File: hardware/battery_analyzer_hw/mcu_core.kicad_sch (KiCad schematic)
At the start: 10 parts, among them SW1 SW_Push, SW2 SW_Push, U3 ESP32-S3-WROOM-1

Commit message: feat(hw): add RJ45 slave ports, isolated 1-Wire and PWM routing fix(hw): split I2C into UI and PWR buses to prevent PID blocking
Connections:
- net 1W_CH0: now reaches U3.12 (IO8)
- net 1W_CH1: now reaches U3.17 (IO9)
- net 1W_CH2: now reaches U3.18 (IO10)
- net 1W_CH3: now reaches U3.19 (IO11)
- net ADC_ALERT: now reaches U3.24 (IO47)
- net PWM_CH0: now reaches U3.31 (IO38)
- net PWM_CH1: now reaches U3.32 (IO39)
- net PWM_CH2: now reaches U3.33 (IO40)
- net PWM_CH3: now reaches U3.34 (IO41)
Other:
- moved on the sheet: R5, R6
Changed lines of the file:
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@@
+	(wire
+		(pts
+			(xy 143.51 110.49) (xy 151.13 110.49)
+		)
+		(stroke
+			(width 0)
+			(type default)
+		)
+	)
+	(wire
+		(pts
+			(xy 143.51 105.41) (xy 151.13 105.41)
+		)
+		(stroke
+			(width 0)
+			(type default)
+		)
+	)
 	(wire
 		(pts
@@
 	(wire
 		(pts
-			(xy 196.85 133.35) (xy 196.85 118.11)
-		)
-		(stroke
-			(width 0)
-			(type default)
-		)
-	)
-	(wire
-		(pts
-			(xy 191.77 133.35) (xy 191.77 120.65)
+			(xy 222.25 134.62) (xy 222.25 118.11)
+		)
+		(stroke
+			(width 0)
+			(type default)
+		)
+	)
+	(wire
+		(pts
+			(xy 217.17 134.62) (xy 217.17 120.65)
 		)
 		(stroke
@@
 	(wire
 		(pts
+			(xy 181.61 110.49) (xy 190.5 110.49)
+		)
+		(stroke
+			(width 0)
+			(type default)
+		)
+	)
+	(wire
+		(pts
 			(xy 115.57 74.93) (xy 115.57 82.55)
 		)
@@
 	(wire
 		(pts
-			(xy 191.77 140.97) (xy 191.77 153.67)
+			(xy 217.17 142.24) (xy 217.17 154.94)
 		)
 		(stroke
@@
 	(wire
 		(pts
+			(xy 181.61 105.41) (xy 190.5 105.41)
+		)
+		(stroke
+			(width 0)
+			(type default)
+		)
+	)
+	(wire
+		(pts
 			(xy 115.57 45.72) (xy 115.57 46.99)
 		)
@@
 	(wire
 		(pts
+			(xy 181.61 113.03) (xy 190.5 113.03)
+		)
+		(stroke
+			(width 0)
+			(type default)
+		)
+	)
+	(wire
+		(pts
 			(xy 143.51 123.19) (xy 151.13 123.19)
 		)
@@
 	(wire
 		(pts
-			(xy 196.85 118.11) (xy 181.61 118.11)
+			(xy 143.51 107.95) (xy 151.13 107.95)
+		)
+		(stroke
+			(width 0)
+			(type default)
+		)
+	)
+	(wire
+		(pts
+			(xy 222.25 118.11) (xy 181.61 118.11)
 		)
 		(stroke
@@
 	(wire
 		(pts
-			(xy 191.77 120.65) (xy 181.61 120.65)
+			(xy 217.17 120.65) (xy 181.61 120.65)
 		)
 		(stroke
@@
 	(wire
 		(pts
-			(xy 196.85 140.97) (xy 196.85 153.67)
+			(xy 181.61 107.95) (xy 190.5 107.95)
+		)
+		(stroke
+			(width 0)
+			(type default)
+		)
+	)
+	(wire
+		(pts
+			(xy 143.51 113.03) (xy 151.13 113.03)
+		)
+		(stroke
+			(width 0)
+			(type default)
+		)
+	)
+	(wire
+		(pts
+			(xy 222.25 142.24) (xy 222.25 154.94)
 		)
 		(stroke
@@
 		(pts
 			(xy 109.22 57.15) (xy 102.87 57.15)
+		)
+		(stroke
+			(width 0)
+			(type default)
+		)
+	)
+	(wire
+		(pts
+			(xy 181.61 123.19) (xy 189.23 123.19)
 		)
 		(stroke
@@
 		)
 	)
+	(hierarchical_label "PWM_CH0"
+		(shape bidirectional)
+		(at 190.5 105.41 0)
+		(effects
+			(font
+				(size 1.27 1.27)
+			)
+			(justify left)
+		)
+	)
 	(hierarchical_label "ENC_B"
 		(shape bidirectional)
@@
 		)
 	)
+	(hierarchical_label "PWM_CH1"
+		(shape bidirectional)
+		(at 190.5 107.95 0)
+		(effects
+			(font
+				(size 1.27 1.27)
+			)
+			(justify left)
+		)
+	)
+	(hierarchical_label "1W_CH0"
+		(shape bidirectional)
+		(at 143.51 105.41 180)
+		(effects
+			(font
+				(size 1.27 1.27)
+			)
+			(justify right)
+		)
+	)
 	(hierarchical_label "BTN_TARE"
 		(shape bidirectional)
@@
 		)
 	)
+	(hierarchical_label "1W_CH3"
+		(shape bidirectional)
+		(at 143.51 113.03 180)
+		(effects
+			(font
+				(size 1.27 1.27)
+			)
+			(justify right)
+		)
+	)
 	(hierarchical_label "USB_D-"
 		(shape bidirectional)
@@
 			)
 			(justify right)
+		)
+	)
+	(hierarchical_label "PWM_CH2"
+		(shape bidirectional)
+		(at 190.5 110.49 0)
+		(effects
+			(font
+				(size 1.27 1.27)
+			)
+			(justify left)
+		)
+	)
+	(hierarchical_label "1W_CH1"
+		(shape bidirectional)
+		(at 143.51 107.95 180)
+		(effects
+			(font
+				(size 1.27 1.27)
+			)
+			(justify right)
+		)
+	)
+	(hierarchical_label "ADC_ALERT"
+		(shape bidirectional)
+		(at 189.23 123.19 0)
+		(effects
+			(font
+				(size 1.27 1.27)
+			)
+			(justify left)
+		)
+	)
+	(hierarchical_label "1W_CH2"
+		(shape bidirectional)
+		(at 143.51 110.49 180)
+		(effects
+			(font
+				(size 1.27 1.27)
+			)
+			(justify right)
+		)
+	)
+	(hierarchical_label "PWM_CH3"
+		(shape bidirectional)
+		(at 190.5 113.03 0)
+		(effects
+			(font
+				(size 1.27 1.27)
+			)
+			(justify left)
 		)
 	)
@@
 	(symbol
 		(lib_id "Device:R")
-		(at 196.85 137.16 0)
+		(at 222.25 138.43 0)
 		(unit 1)
 		(body_style 1)
@@
 		(fields_autoplaced yes)
 		(property "Reference" "R5"
-			(at 199.39 135.8899 0)
+			(at 224.79 137.1599 0)
 			(show_name no)
 			(do_not_autoplace no)
@@
 		)
 		(property "Value" "10k"
-			(at 199.39 138.4299 0)
+			(at 224.79 139.6999 0)
 			(show_name no)
 			(do_not_autoplace no)
@@
 		)
 		(property "Footprint" ""
-			(at 195.072 137.16 90)
+			(at 220.472 138.43 90)
 			(hide yes)
 			(show_name no)
@@
 		)
 		(property "Datasheet" ""
-			(at 196.85 137.16 0)
+			(at 222.25 138.43 0)
 			(hide yes)
 			(show_name no)
@@
 		)
 		(property "Description" "Resistor"
-			(at 196.85 137.16 0)
+			(at 222.25 138.43 0)
 			(hide yes)
 			(show_name no)
@@
 	(symbol
 		(lib_id "power:GND")
-		(at 196.85 153.67 0)
+		(at 222.25 154.94 0)
 		(unit 1)
 		(body_style 1)
@@
 		(fields_autoplaced yes)
 		(property "Reference" "#PWR022"
-			(at 196.85 160.02 0)
+			(at 222.25 161.29 0)
 			(hide yes)
 			(show_name no)
@@
 		)
 		(property "Value" "GND"
-			(at 196.85 158.75 0)
+			(at 222.25 160.02 0)
 			(show_name no)
 			(do_not_autoplace no)
@@
 		)
 		(property "Footprint" ""
-			(at 196.85 153.67 0)
+			(at 222.25 154.94 0)
 			(hide yes)
 			(show_name no)
@@
 		)
 		(property "Datasheet" ""
-			(at 196.85 153.67 0)
+			(at 222.25 154.94 0)
 			(hide yes)
 			(show_name no)
@@
 		)
 		(property "Description" "Power symbol creates a global label with name \"GND\" , ground"
-			(at 196.85 153.67 0)
+			(at 222.25 154.94 0)
 			(hide yes)
 			(show_name no)
@@
 	(symbol
 		(lib_id "Device:R")
-		(at 191.77 137.16 0)
+		(at 217.17 138.43 0)
 		(mirror y)
 		(unit 1)
@@
 		(fields_autoplaced yes)
 		(property "Reference" "R6"
-			(at 189.23 135.8899 0)
+			(at 214.63 137.1599 0)
 			(show_name no)
 			(do_not_autoplace no)
@@
 		)
 		(property "Value" "10k"
-			(at 189.23 138.4299 0)
+			(at 214.63 139.6999 0)
 			(show_name no)
 			(do_not_autoplace no)
@@
 		)
 		(property "Footprint" ""
-			(at 193.548 137.16 90)
+			(at 218.948 138.43 90)
 			(hide yes)
 			(show_name no)
@@
 		)
 		(property "Datasheet" ""
-			(at 191.77 137.16 0)
+			(at 217.17 138.43 0)
 			(hide yes)
 			(show_name no)
@@
 		)
 		(property "Description" "Resistor"
-			(at 191.77 137.16 0)
+			(at 217.17 138.43 0)
 			(hide yes)
 			(show_name no)
@@
 	(symbol
 		(lib_id "power:GND")
-		(at 191.77 153.67 0)
+		(at 217.17 154.94 0)
 		(unit 1)
 		(body_style 1)
@@
 		(fields_autoplaced yes)
 		(property "Reference" "#PWR021"
-			(at 191.77 160.02 0)
+			(at 217.17 161.29 0)
 			(hide yes)
 			(show_name no)
@@
 		)
 		(property "Value" "GND"
-			(at 191.77 158.75 0)
+			(at 217.17 160.02 0)
 			(show_name no)
 			(do_not_autoplace no)
@@
 		)
 		(property "Footprint" ""
-			(at 191.77 153.67 0)
+			(at 217.17 154.94 0)
 			(hide yes)
 			(show_name no)
@@
 		)
 		(property "Datasheet" ""
-			(at 191.77 153.67 0)
+			(at 217.17 154.94 0)
 			(hide yes)
 			(show_name no)
@@
 		)
 		(property "Description" "Power symbol creates a global label with name \"GND\" , ground"
-			(at 191.77 153.67 0)
-			(hide yes)
-			(show_name no)
+			(at 217.17 154.94 0)
+			(hide yes)
+			(show_name no)

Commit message: refactor(hw): upgrade RJ45 to shielded, repurpose pin 1 for fan PWM fix(hw): optimize RJ45 pinout for T568B twisted pairs
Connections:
- net FAN_CH0: now reaches U3.20 (IO12)
- net FAN_CH1: now reaches U3.21 (IO13)
- net FAN_CH2: now reaches U3.22 (IO14)
- net FAN_CH3: now reaches U3.23 (IO21)
- net I2C_PWR_SDA: now reaches U3.6 (IO6)
- net I2C_PWR_SCL: now reaches U3.7 (IO7)
- net I2C_SCL renamed I2C_UI_SCL
- net I2C_SDA renamed I2C_UI_SDA
- no-connect marks 0 -> 10
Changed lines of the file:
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@@
 		(color 0 0 0 0)
 	)
+	(no_connect
+		(at 181.61 100.33)
+	)
+	(no_connect
+		(at 181.61 102.87)
+	)
+	(no_connect
+		(at 181.61 115.57)
+	)
+	(no_connect
+		(at 151.13 90.17)
+	)
+	(no_connect
+		(at 181.61 82.55)
+	)
+	(no_connect
+		(at 181.61 97.79)
+	)
+	(no_connect
+		(at 151.13 92.71)
+	)
+	(no_connect
+		(at 181.61 80.01)
+	)
+	(no_connect
+		(at 151.13 87.63)
+	)
+	(no_connect
+		(at 181.61 125.73)
+	)
 	(wire
 		(pts
@@
 	(wire
 		(pts
+			(xy 143.51 118.11) (xy 151.13 118.11)
+		)
+		(stroke
+			(width 0)
+			(type default)
+		)
+	)
+	(wire
+		(pts
 			(xy 102.87 45.72) (xy 104.14 45.72)
 		)
@@
 	(wire
 		(pts
+			(xy 143.51 120.65) (xy 151.13 120.65)
+		)
+		(stroke
+			(width 0)
+			(type default)
+		)
+	)
+	(wire
+		(pts
 			(xy 115.57 74.93) (xy 115.57 82.55)
 		)
@@
 	(wire
 		(pts
+			(xy 143.51 100.33) (xy 151.13 100.33)
+		)
+		(stroke
+			(width 0)
+			(type default)
+		)
+	)
+	(wire
+		(pts
+			(xy 143.51 102.87) (xy 151.13 102.87)
+		)
+		(stroke
+			(width 0)
+			(type default)
+		)
+	)
+	(wire
+		(pts
 			(xy 146.05 59.69) (xy 146.05 64.77)
 		)
@@
 	(wire
 		(pts
+			(xy 143.51 115.57) (xy 151.13 115.57)
+		)
+		(stroke
+			(width 0)
+			(type default)
+		)
+	)
+	(wire
+		(pts
 			(xy 105.41 97.79) (xy 105.41 107.95)
 		)
@@
 	(wire
 		(pts
+			(xy 181.61 95.25) (xy 189.23 95.25)
+		)
+		(stroke
+			(width 0)
+			(type default)
+		)
+	)
+	(wire
+		(pts
 			(xy 181.61 123.19) (xy 189.23 123.19)
 		)
@@
 		)
 	)
-	(hierarchical_label "I2C_SCL"
+	(hierarchical_label "I2C_UI_SCL"
 		(shape bidirectional)
 		(at 143.51 97.79 180)
@@
 		)
 	)
-	(hierarchical_label "I2C_SDA"
+	(hierarchical_label "FAN_CH3"
+		(shape bidirectional)
+		(at 189.23 95.25 0)
+		(effects
+			(font
+				(size 1.27 1.27)
+			)
+			(justify left)
+		)
+	)
+	(hierarchical_label "I2C_UI_SDA"
 		(shape bidirectional)
 		(at 143.51 95.25 180)
@@
 		)
 	)
+	(hierarchical_label "FAN_CH0"
+		(shape bidirectional)
+		(at 143.51 115.57 180)
+		(effects
+			(font
+				(size 1.27 1.27)
+			)
+			(justify right)
+		)
+	)
 	(hierarchical_label "ADC_ALERT"
 		(shape bidirectional)
@@
 		)
 	)
+	(hierarchical_label "FAN_CH1"
+		(shape bidirectional)
+		(at 143.51 118.11 180)
+		(effects
+			(font
+				(size 1.27 1.27)
+			)
+			(justify right)
+		)
+	)
+	(hierarchical_label "FAN_CH2"
+		(shape bidirectional)
+		(at 143.51 120.65 180)
+		(effects
+			(font
+				(size 1.27 1.27)
+			)
+			(justify right)
+		)
+	)
 	(hierarchical_label "1W_CH2"
 		(shape bidirectional)
@@
 		)
 	)
+	(hierarchical_label "I2C_PWR_SCL"
+		(shape bidirectional)
+		(at 143.51 102.87 180)
+		(effects
+			(font
+				(size 1.27 1.27)
+			)
+			(justify right)
+		)
+	)
+	(hierarchical_label "I2C_PWR_SDA"
+		(shape bidirectional)
+		(at 143.51 100.33 180)
+		(effects
+			(font
+				(size 1.27 1.27)
+			)
+			(justify right)
+		)
+	)

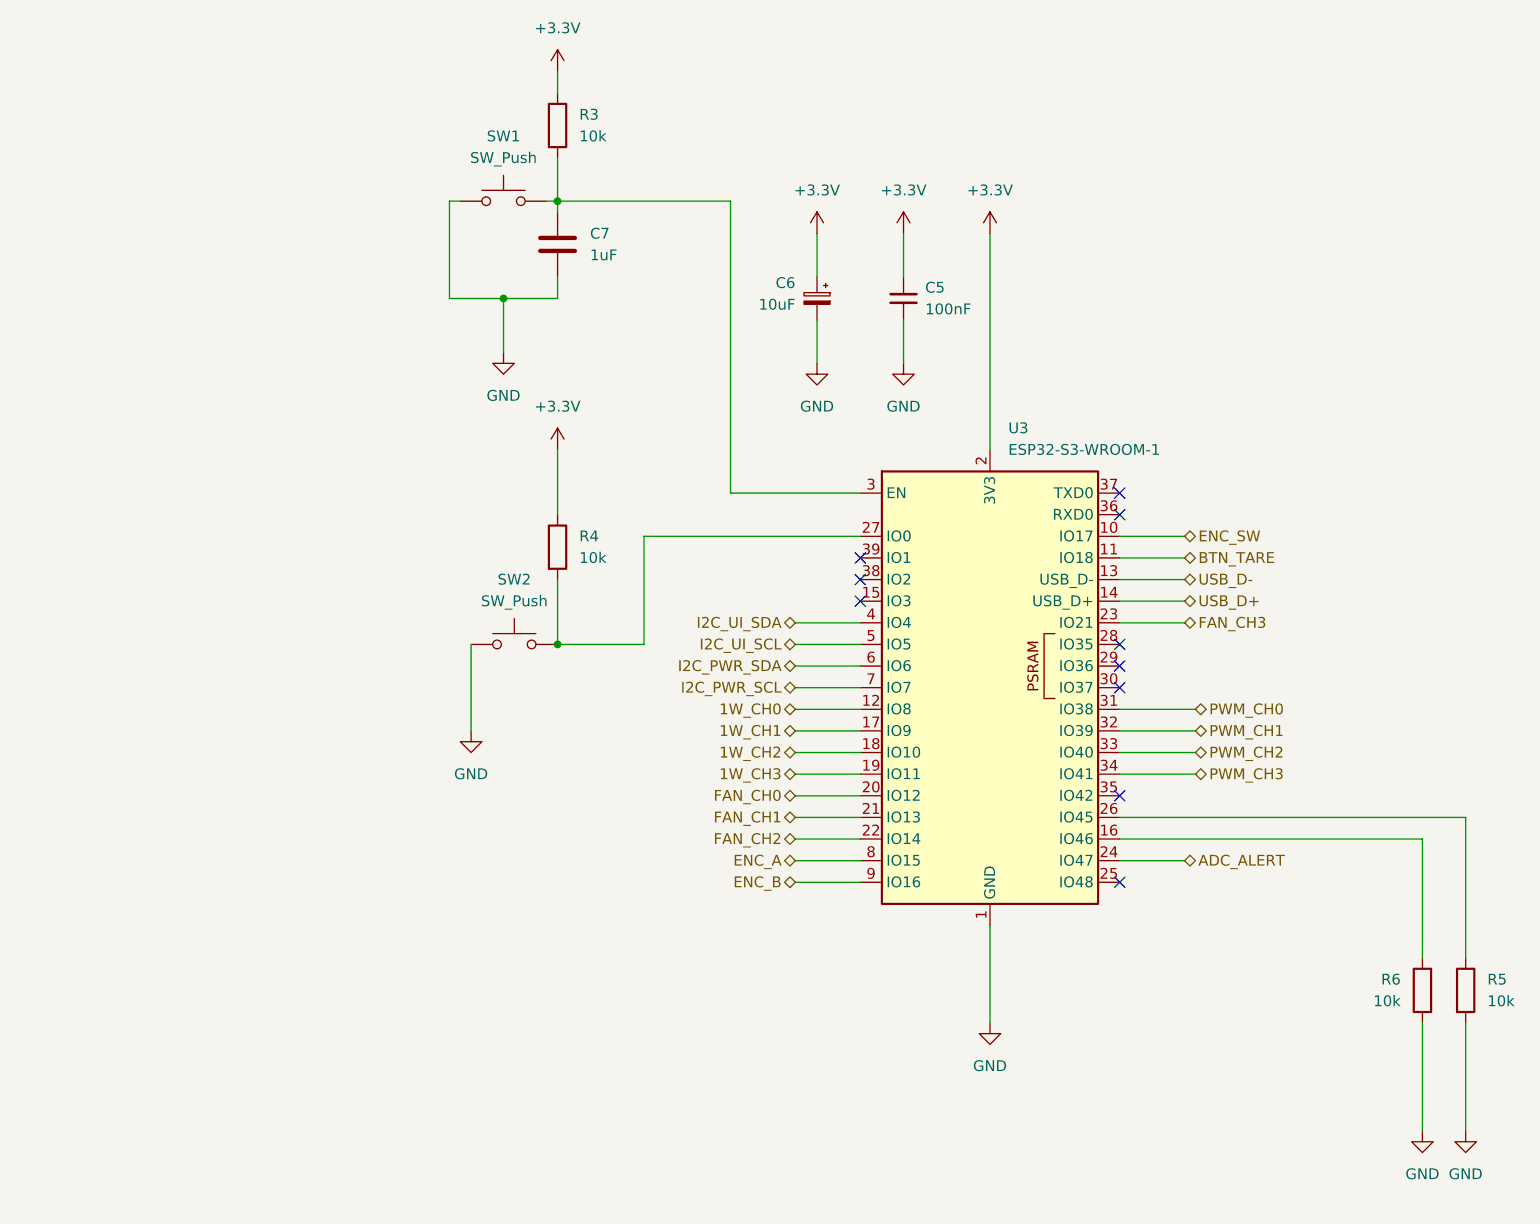
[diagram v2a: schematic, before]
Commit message: hw(master): fix footprints, apply HandSolder and Tantalum
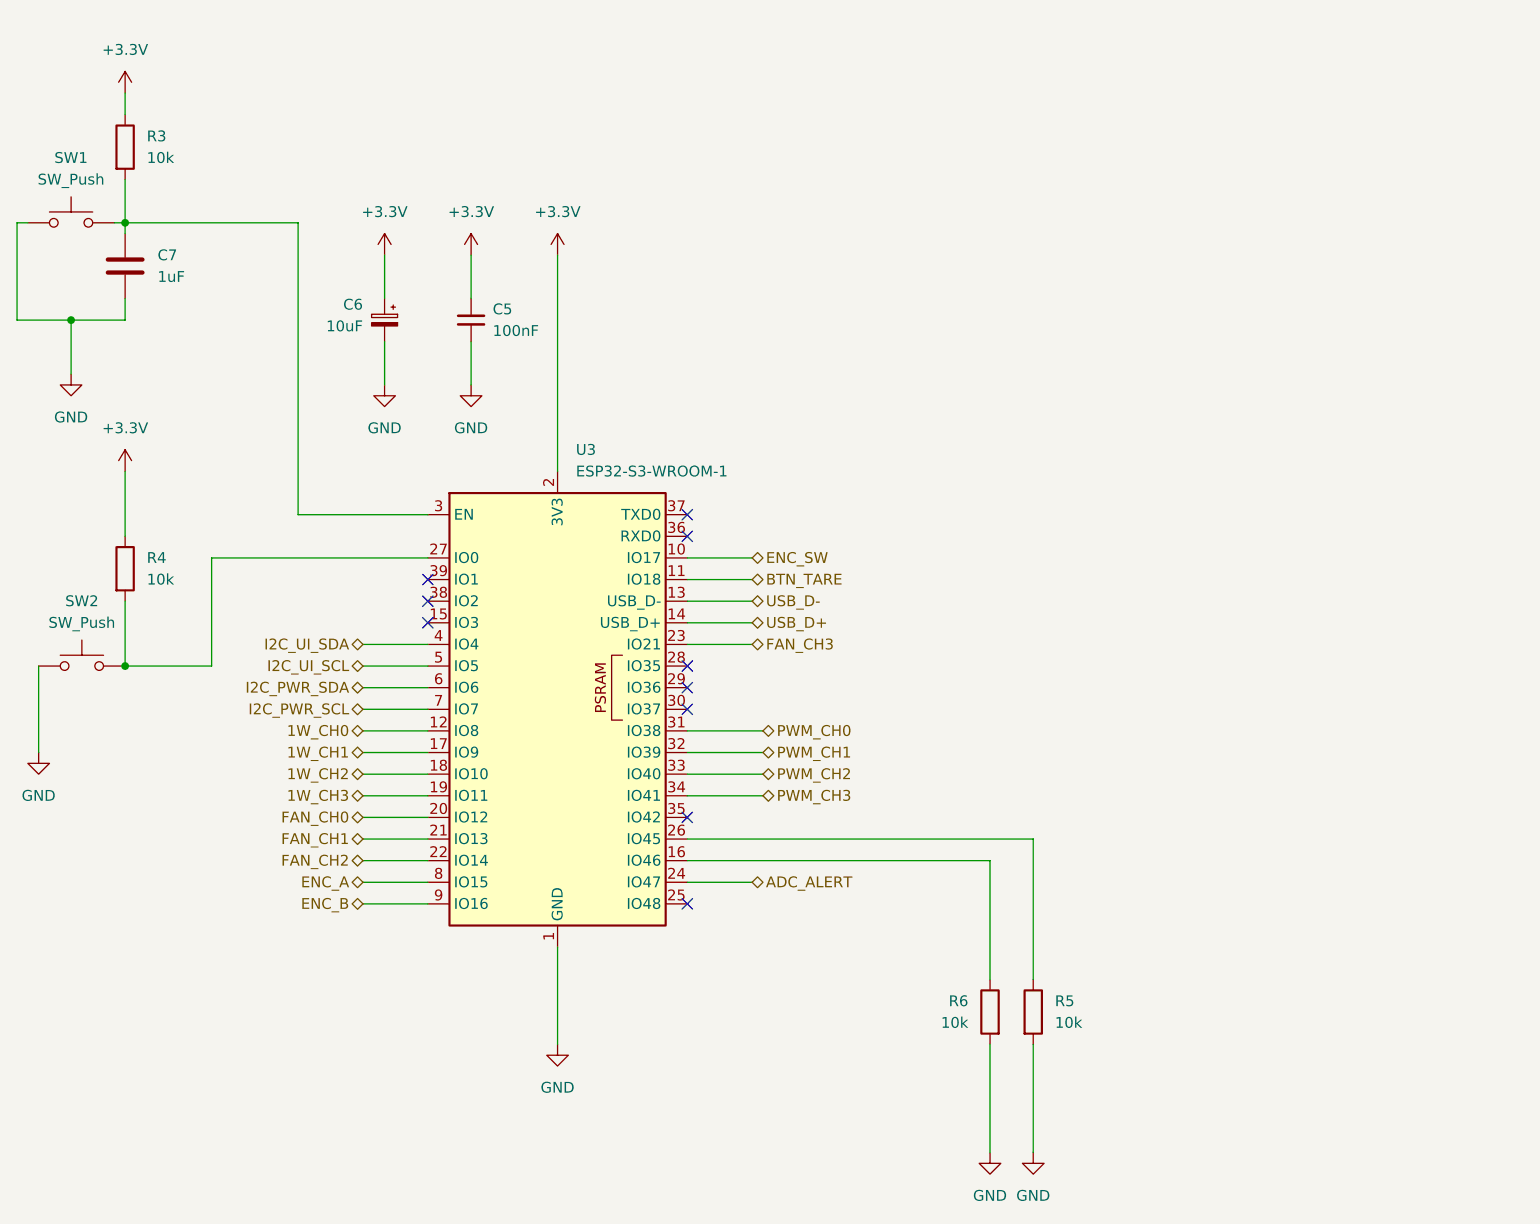
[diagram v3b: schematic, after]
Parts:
- C5: footprint Package_LCC:PLCC-44_16.6x16.6mm_P1.27mm -> Capacitor_SMD:C_0805_2012Metric_Pad1.18x1.45mm_HandSolder
- C6: footprint (none) -> Capacitor_Tantalum_SMD:CP_EIA-3216-18_Kemet-A_HandSolder
- C7: footprint (none) -> Capacitor_SMD:C_0805_2012Metric_Pad1.18x1.45mm_HandSolder
- R3, R4, R5, R6: footprint (none) -> Resistor_SMD:R_0805_2012Metric_Pad1.20x1.40mm_HandSolder
- SW1: footprint (none) -> Button_Switch_THT:SW_PUSH_6mm
- SW2: footprint Button_Switch_SMD:Nidec_Copal_CAS-120A -> Button_Switch_THT:SW_PUSH_6mm
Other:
- moved on the sheet: C5, C6, C7, R3, R4, R5, R6, SW1, SW2, U3
